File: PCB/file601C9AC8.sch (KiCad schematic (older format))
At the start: 30 parts, among them IC6 WM8960CGEFL_V, J1 615008144221, J2 1725672, J4 SJ-3566AN, J9 MJ-3523-SMT, Y1 TSX-3225_24.0000MF18X-C

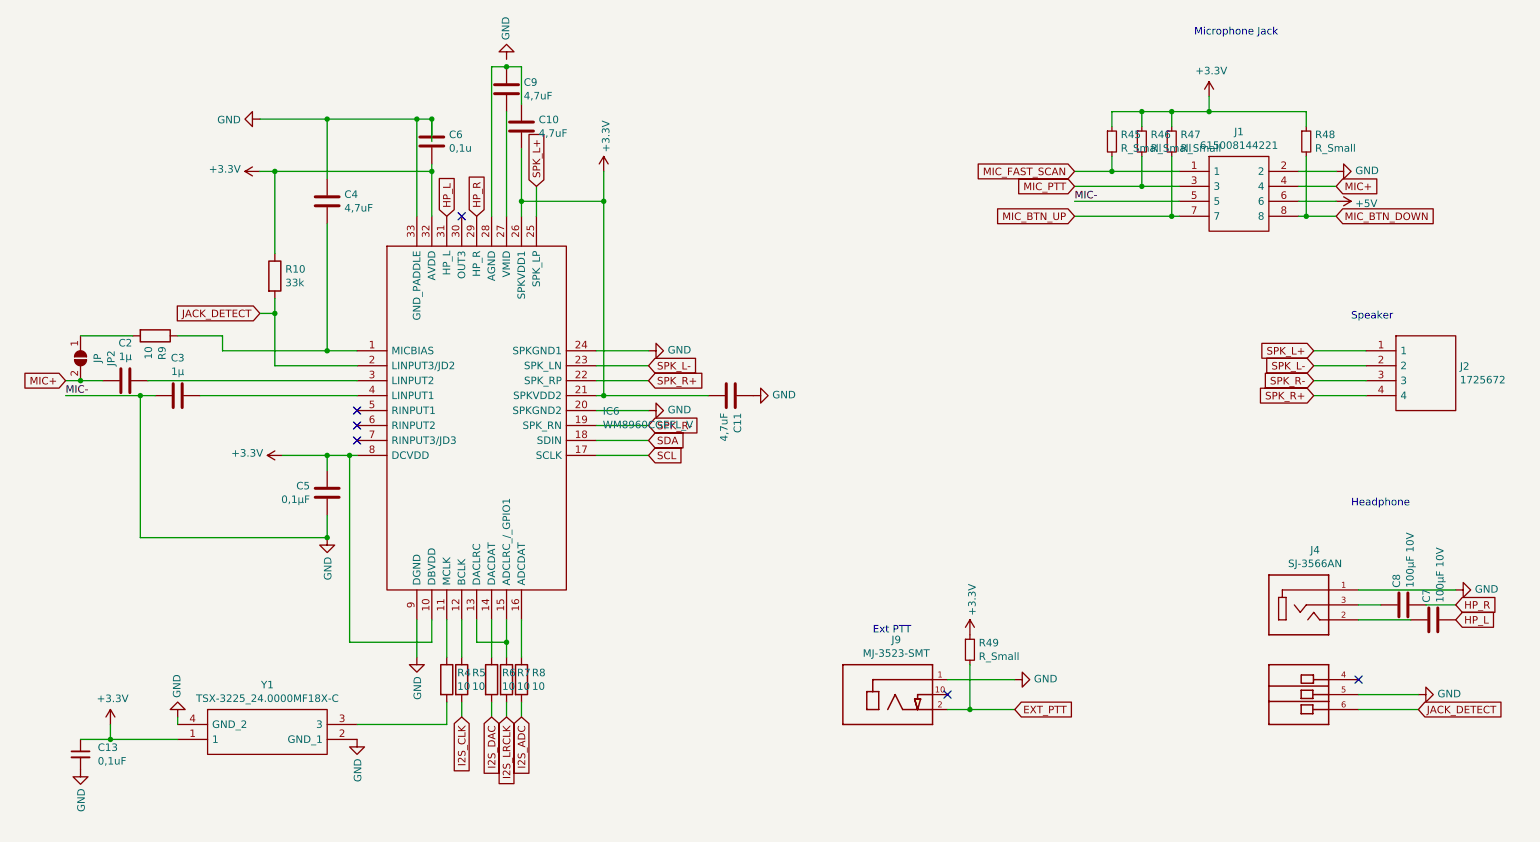
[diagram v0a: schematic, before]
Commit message: Cleaned up repository. Created a BOM in iBOM Format.
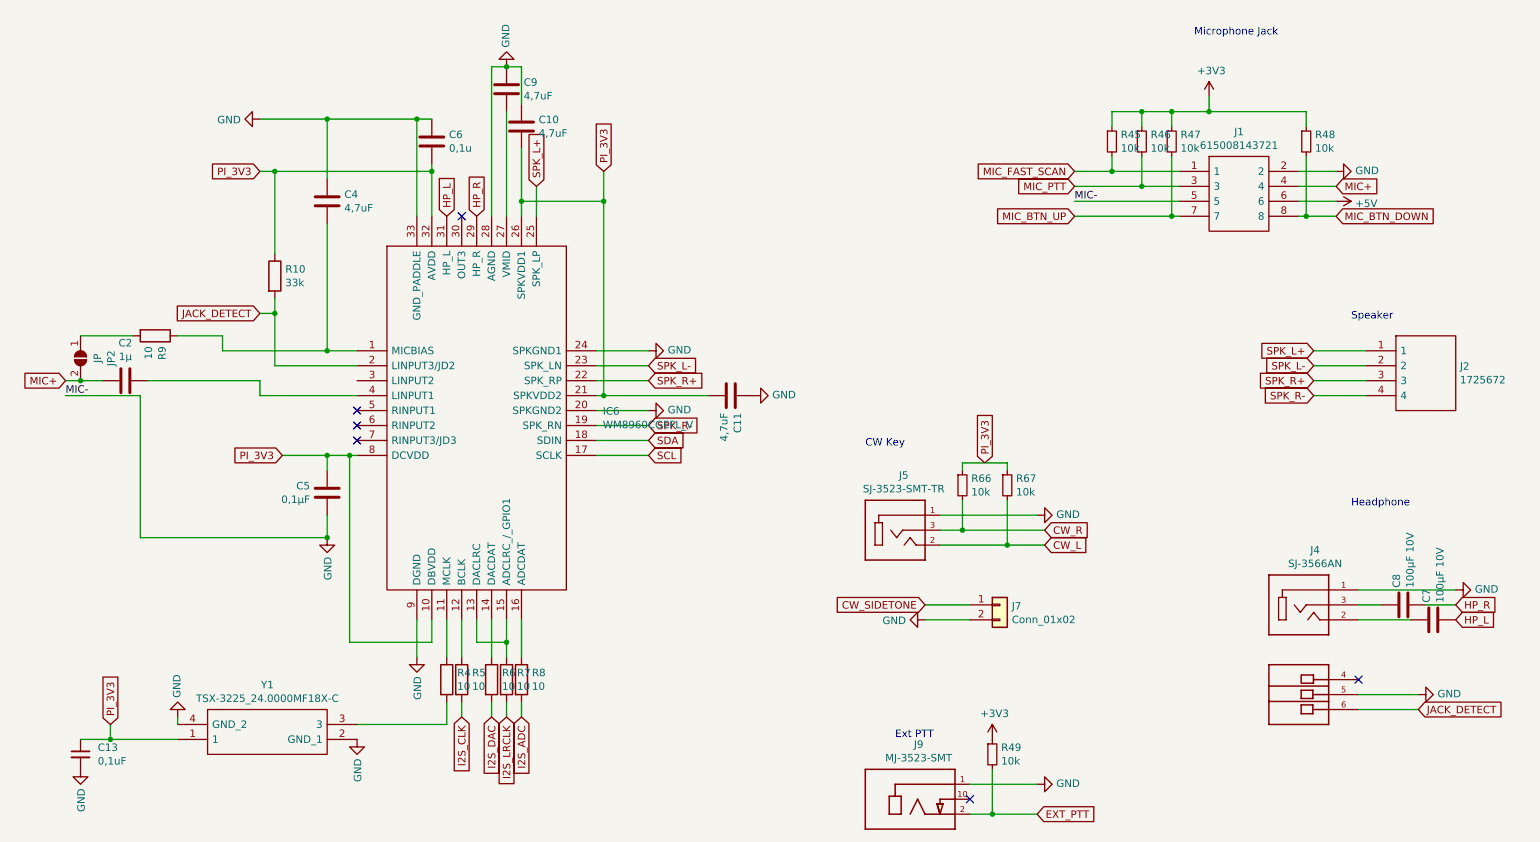
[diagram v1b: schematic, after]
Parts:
- removed C3: 1µ, Capacitor_SMD:C_0805_2012Metric_Pad1.15x1.40mm_HandSolder, symbol Device:C
- removed J1: 615008144221, 615008144221, symbol SamacSys_Parts:615008144221
- added J1: 615008143721, 615008143721, symbol SamacSys_Parts:615008143721
- added J5: SJ-3523-SMT-TR, CUI_SJ-3523-SMT-TR, symbol CUI_Devices:SJ-3523-SMT-TR
- added J7: Conn_01x02, Connector_PinHeader_2.54mm:PinHeader_1x02_P2.54mm_Horizontal, symbol Connector_Generic:Conn_01x02
- added R66, R67: 10k, Resistor_SMD:R_0805_2012Metric_Pad1.15x1.40mm_HandSolder, symbol Device:R_Small
- R45, R46, R47, R48, R49: value R_Small -> 10k
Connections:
- net +3V3: no longer C10.2, C11.2, C13.1, C5.1, C6.2, IC6.10 (DBVDD), IC6.21 (SPKVDD2), IC6.26 (SPKVDD1), IC6.32 (AVDD), IC6.8 (DCVDD), R10.1, Y1.1
- net +5V: now also J1.6
- net GND: now also C10.1, C9.1, IC6.28 (AGND), J1.2, J1.5, J5.1, J7.2 (Pin_2)
- net MIC+: now also J1.4
- net MIC_BTN_DOWN: now also J1.8
- net MIC_BTN_UP: now also J1.7
- net MIC_FAST_SCAN: now also J1.1
- net MIC_PTT: now also J1.3
- net SPK_R+: now also J2.3; no longer J2.4
- net SPK_R-: now also J2.4; no longer J2.3
- net at IC6.3 (LINPUT2): no longer C2.2
- net at IC6.4 (LINPUT1): now also C2.2
- new net CW_L: J5.2, R67.2
- new net CW_R: J5.3, R66.2
- new net CW_SIDETONE: J7.1 (Pin_1)
- new net PI_3V3: C10.2, C11.2, C13.1, C5.1, C6.2, IC6.10 (DBVDD), IC6.21 (SPKVDD2), IC6.26 (SPKVDD1), IC6.32 (AVDD), IC6.8 (DCVDD), R10.1, R66.1, R67.1, Y1.1
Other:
- note added: "CW Key"
- moved on the sheet: J9, R49

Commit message: Completed parts details on schematics and recreated gerbers and bom.
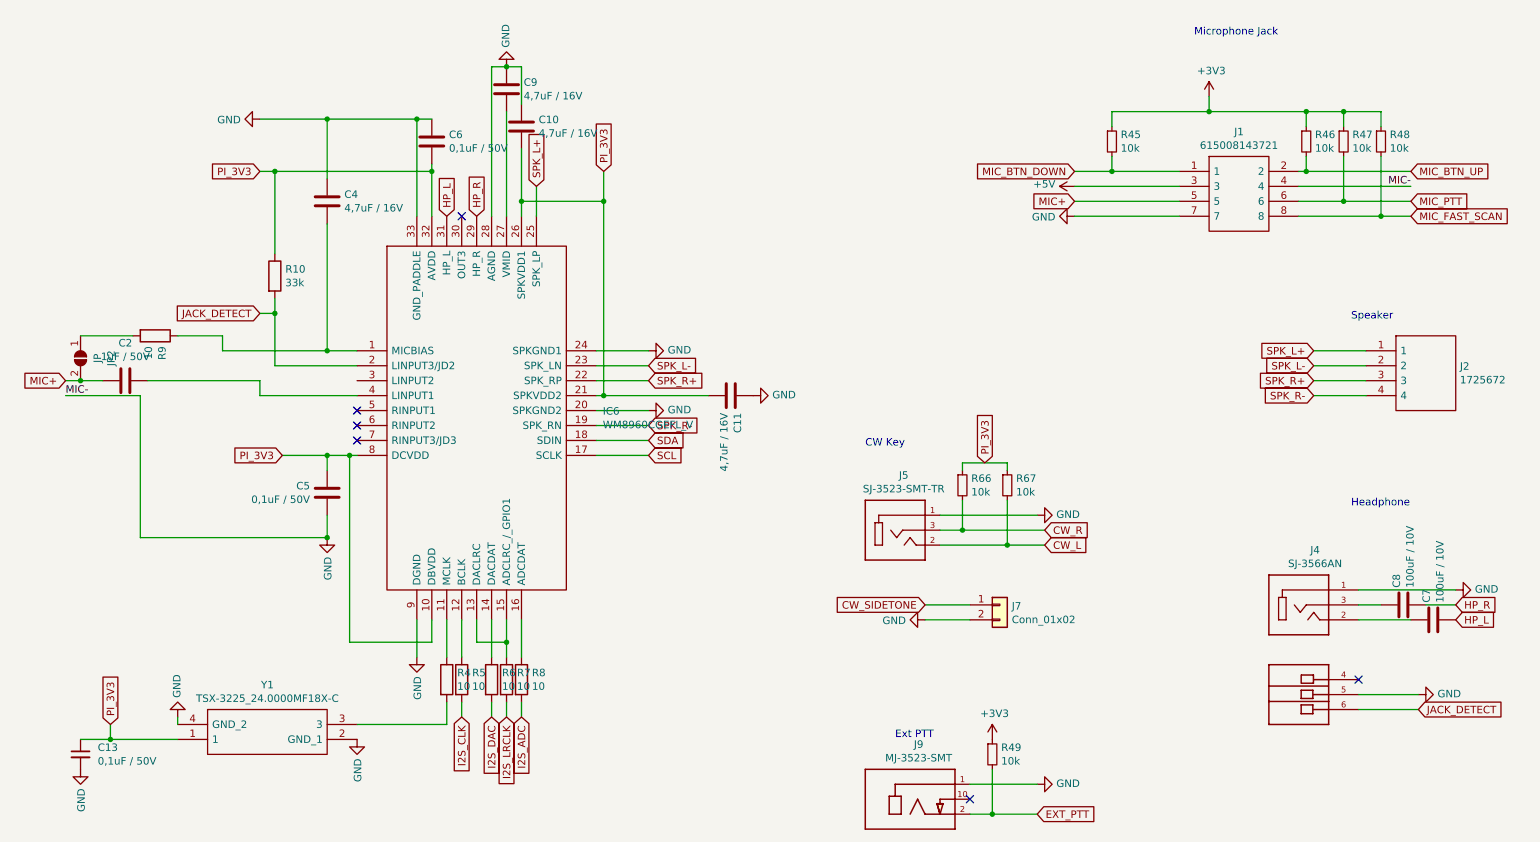
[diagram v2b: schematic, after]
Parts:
- C10, C11, C4, C9: value 4,7uF -> 4,7uF / 16V; LCSC (none) -> C1746; Manufacturer_Name (none) -> Samsung Electro-Mechanics; Manufacturer_Part_Number (none) -> CL21A475KOFNNNE; Mouser Part Number (none) -> 187-CL21A475KOFNNNE
- C13: value 0,1uF -> 0,1uF / 50V; LCSC C62912 -> C62912; Manufacturer_Part_Number CL21B104JBCNNNC -> CL21B104KBCSFNC; Mouser Part Number (none) -> 187-CL21B104KBCSFNC
- C2: value 1µ -> 1uF / 50V; LCSC (none) -> C28323; Manufacturer_Name (none) -> Samsung Electro-Mechanics; Manufacturer_Part_Number (none) -> CL21B105KBFNNNE; Mouser Part Number (none) -> 187-CL21B105KBFNNNE
- C5: value 0,1µF -> 0,1uF / 50V; LCSC (none) -> C62912; Manufacturer_Name (none) -> Samsung Electro-Mechanics; Manufacturer_Part_Number (none) -> CL21B104KBCSFNC; Mouser Part Number (none) -> 187-CL21B104KBCSFNC
- C6: value 0,1u -> 0,1uF / 50V; LCSC (none) -> C62912; Manufacturer_Name (none) -> Samsung Electro-Mechanics; Manufacturer_Part_Number (none) -> CL21B104KBCSFNC; Mouser Part Number (none) -> 187-CL21B104KBCSFNC
- C7, C8: value 100µF 10V -> 100uF / 10V; LCSC (none) -> C307523; Manufacturer_Name (none) -> Samsung Electro-Mechanics; Manufacturer_Part_Number (none) -> CL21A106KPFNNNG; Mouser Part Number (none) -> 187-CL21A106KPFNNNG
- IC6: LCSC (none) -> C18752
- J4: Manufacturer_Name (none) -> CUI Devices; Manufacturer_Part_Number (none) -> SJ-3566AN; Mouser Part Number (none) -> 490-SJ-3566AN
- J5: Manufacturer_Name (none) -> CUI Devices; Manufacturer_Part_Number (none) -> SJ-3523-SMT-TR; Mouser Part Number (none) -> 490-SJ-3523-SMT-TR
- J7: Manufacturer_Name (none) -> Amphenol; Manufacturer_Part_Number (none) -> 10129379-902001BLF; Mouser Part Number (none) -> 649-1012937990201BLF
- J9: Manufacturer_Name (none) -> CUI Devices; Manufacturer_Part_Number (none) -> MJ-3523-SMT-TR; Mouser Part Number (none) -> 490-MJ-3523-SMT-TR
- R10: LCSC (none) -> C17633; Manufacturer_Name (none) -> Vishay; Manufacturer_Part_Number (none) -> CRCW080533K0FKEA; Mouser Part Number (none) -> 71-CRCW0805-33K-E3
- R4, R5, R6, R7, R8, R9: LCSC (none) -> C17415; Manufacturer_Name (none) -> Vishay; Manufacturer_Part_Number (none) -> CRCW080510R0FKEB; Mouser Part Number (none) -> 71-CRCW080510R0FKEB
- R45, R46, R47, R48, R49, R66, R67: LCSC (none) -> C17414; Manufacturer_Name (none) -> Vishay; Manufacturer_Part_Number (none) -> CRCW080510K0FKEAC; Mouser Part Number (none) -> 71-CRCW080510K0FKEAC
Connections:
- net +5V: now also J1.3; no longer J1.6
- net GND: now also J1.4, J1.7; no longer J1.2, J1.5
- net MIC+: now also J1.5; no longer J1.4
- net MIC_BTN_DOWN: now also J1.1, R45.2; no longer J1.8, R48.2
- net MIC_BTN_UP: now also J1.2, R46.2; no longer J1.7, R47.2
- net MIC_FAST_SCAN: now also J1.8, R48.2; no longer J1.1, R45.2
- net MIC_PTT: now also J1.6, R47.2; no longer J1.3, R46.2
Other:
- moved on the sheet: R46, R47, R48

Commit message: Refactored JLC Part Numbers. And replaced 100uF capacitors with 1206 sized parts.
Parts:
- C10, C11, C4, C9: LCSC C1746 -> C1779
- C13, C5, C6: LCSC C62912 -> C49678
- C7, C8: footprint Capacitor_SMD:C_0805_2012Metric_Pad1.15x1.40mm_HandSolder -> Capacitor_SMD:C_1206_3216Metric_Pad1.42x1.75mm_HandSolder; LCSC C307523 -> C84455; Manufacturer_Name Samsung Electro-Mechanics -> Murata Electronics; Manufacturer_Part_Number CL21A106KPFNNNG -> GRM32ER61A107ME20L; Mouser Part Number 187-CL21A106KPFNNNG -> 81-GRM32ER61A107ME0L
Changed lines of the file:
@@
 F 2 "Capacitor_SMD:C_0805_2012Metric_Pad1.15x1.40mm_HandSolder" H 3838 1350 50  0001 C CNN
 F 3 "~" H 3800 1500 50  0001 C CNN
-F 4 "C62912" H 3800 1500 50  0001 C CNN "LCSC"
+F 4 "C49678" H 3800 1500 50  0001 C CNN "LCSC"
 F 5 "Samsung Electro-Mechanics" H 3800 1500 50  0001 C CNN "Manufacturer_Name"
 F 6 "CL21B104KBCSFNC" H 3800 1500 50  0001 C CNN "Manufacturer_Part_Number"
@@
 F 2 "Capacitor_SMD:C_0805_2012Metric_Pad1.15x1.40mm_HandSolder" H 3138 1750 50  0001 C CNN
 F 3 "~" H 3100 1900 50  0001 C CNN
-F 4 "C1746" H 3100 1900 50  0001 C CNN "LCSC"
+F 4 "C1779" H 3100 1900 50  0001 C CNN "LCSC"
 F 5 "Samsung Electro-Mechanics" H 3100 1900 50  0001 C CNN "Manufacturer_Name"
 F 6 "CL21A475KOFNNNE" H 3100 1900 50  0001 C CNN "Manufacturer_Part_Number"
@@
 F 2 "Capacitor_SMD:C_0805_2012Metric_Pad1.15x1.40mm_HandSolder" H 3138 3700 50  0001 C CNN
 F 3 "~" H 3100 3850 50  0001 C CNN
-F 4 "C62912" H 3100 3850 50  0001 C CNN "LCSC"
+F 4 "C49678" H 3100 3850 50  0001 C CNN "LCSC"
 F 5 "Samsung Electro-Mechanics" H 3100 3850 50  0001 C CNN "Manufacturer_Name"
 F 6 "CL21B104KBCSFNC" H 3100 3850 50  0001 C CNN "Manufacturer_Part_Number"
@@
 F 0 "C7" H 10615 4746 50  0000 L CNN
 F 1 "100uF / 10V" H 10615 4655 50  0000 L CNN
-F 2 "Capacitor_SMD:C_0805_2012Metric_Pad1.15x1.40mm_HandSolder" H 10538 4550 50  0001 C CNN
+F 2 "Capacitor_SMD:C_1206_3216Metric_Pad1.42x1.75mm_HandSolder" H 10538 4550 50  0001 C CNN
 F 3 "~" H 10500 4700 50  0001 C CNN
-F 4 "C307523" H 10500 4700 50  0001 C CNN "LCSC"
-F 5 "Samsung Electro-Mechanics" H 10500 4700 50  0001 C CNN "Manufacturer_Name"
-F 6 "CL21A106KPFNNNG" H 10500 4700 50  0001 C CNN "Manufacturer_Part_Number"
-F 7 "187-CL21A106KPFNNNG" H 10500 4700 50  0001 C CNN "Mouser Part Number"
+F 4 "C84455" H 10500 4700 50  0001 C CNN "LCSC"
+F 5 "Murata Electronics" H 10500 4700 50  0001 C CNN "Manufacturer_Name"
+F 6 "GRM32ER61A107ME20L" H 10500 4700 50  0001 C CNN "Manufacturer_Part_Number"
+F 7 "81-GRM32ER61A107ME0L" H 10500 4700 50  0001 C CNN "Mouser Part Number"
 	1    10500 4700
 	0    -1   -1   0
@@
 F 0 "C8" H 10415 4646 50  0000 L CNN
 F 1 "100uF / 10V" H 10415 4555 50  0000 L CNN
-F 2 "Capacitor_SMD:C_0805_2012Metric_Pad1.15x1.40mm_HandSolder" H 10338 4450 50  0001 C CNN
+F 2 "Capacitor_SMD:C_1206_3216Metric_Pad1.42x1.75mm_HandSolder" H 10338 4450 50  0001 C CNN
 F 3 "~" H 10300 4600 50  0001 C CNN
-F 4 "C307523" H 10300 4600 50  0001 C CNN "LCSC"
-F 5 "Samsung Electro-Mechanics" H 10300 4600 50  0001 C CNN "Manufacturer_Name"
-F 6 "CL21A106KPFNNNG" H 10300 4600 50  0001 C CNN "Manufacturer_Part_Number"
-F 7 "187-CL21A106KPFNNNG" H 10300 4600 50  0001 C CNN "Mouser Part Number"
+F 4 "C84455" H 10300 4600 50  0001 C CNN "LCSC"
+F 5 "Murata Electronics" H 10300 4600 50  0001 C CNN "Manufacturer_Name"
+F 6 "GRM32ER61A107ME20L" H 10300 4600 50  0001 C CNN "Manufacturer_Part_Number"
+F 7 "81-GRM32ER61A107ME0L" H 10300 4600 50  0001 C CNN "Mouser Part Number"
 	1    10300 4600
 	0    -1   -1   0
@@
 F 4 "Samsung Electro-Mechanics" H 1450 5600 50  0001 C CNN "Manufacturer_Name"
 F 5 "CL21B104KBCSFNC" H 1450 5600 50  0001 C CNN "Manufacturer_Part_Number"
-F 6 "C62912" H 1450 5600 50  0001 C CNN "LCSC"
+F 6 "C49678" H 1450 5600 50  0001 C CNN "LCSC"
 F 7 "187-CL21B104KBCSFNC" H 1450 5600 50  0001 C CNN "Mouser Part Number"
 	1    1450 5600
@@
 F 2 "Capacitor_SMD:C_0805_2012Metric_Pad1.15x1.40mm_HandSolder" H 5838 3050 50  0001 C CNN
 F 3 "~" H 5800 3200 50  0001 C CNN
-F 4 "C1746" H 5800 3200 50  0001 C CNN "LCSC"
+F 4 "C1779" H 5800 3200 50  0001 C CNN "LCSC"
 F 5 "Samsung Electro-Mechanics" H 5800 3200 50  0001 C CNN "Manufacturer_Name"
 F 6 "CL21A475KOFNNNE" H 5800 3200 50  0001 C CNN "Manufacturer_Part_Number"
@@
 F 2 "Capacitor_SMD:C_0805_2012Metric_Pad1.15x1.40mm_HandSolder" H 4338 1000 50  0001 C CNN
 F 3 "~" H 4300 1150 50  0001 C CNN
-F 4 "C1746" H 4300 1150 50  0001 C CNN "LCSC"
+F 4 "C1779" H 4300 1150 50  0001 C CNN "LCSC"
 F 5 "Samsung Electro-Mechanics" H 4300 1150 50  0001 C CNN "Manufacturer_Name"
 F 6 "CL21A475KOFNNNE" H 4300 1150 50  0001 C CNN "Manufacturer_Part_Number"
@@
 F 2 "Capacitor_SMD:C_0805_2012Metric_Pad1.15x1.40mm_HandSolder" H 4438 1250 50  0001 C CNN
 F 3 "~" H 4400 1400 50  0001 C CNN
-F 4 "C1746" H 4400 1400 50  0001 C CNN "LCSC"
+F 4 "C1779" H 4400 1400 50  0001 C CNN "LCSC"
 F 5 "Samsung Electro-Mechanics" H 4400 1400 50  0001 C CNN "Manufacturer_Name"
 F 6 "CL21A475KOFNNNE" H 4400 1400 50  0001 C CNN "Manufacturer_Part_Number"
